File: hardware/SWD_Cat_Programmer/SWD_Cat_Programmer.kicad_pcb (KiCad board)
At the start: 2 copper layers, 40.6 x 28.1 mm, 25 parts, among them J1 DEBUG_OUT, P1 USB_C_Plug_USB2.0, SW1 RST, SW2 BOOT, U1 CH552G, U2 HX9193-33GB

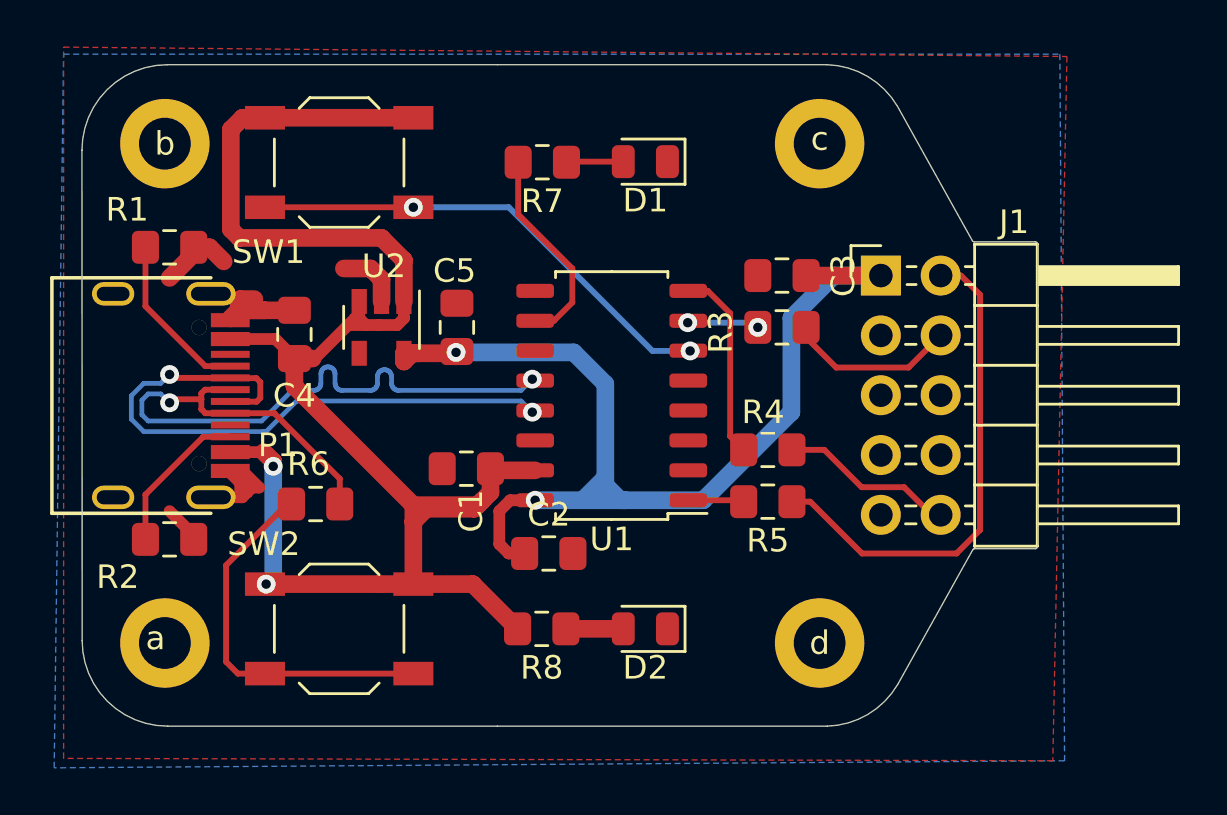
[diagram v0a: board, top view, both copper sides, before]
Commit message: added logos EC
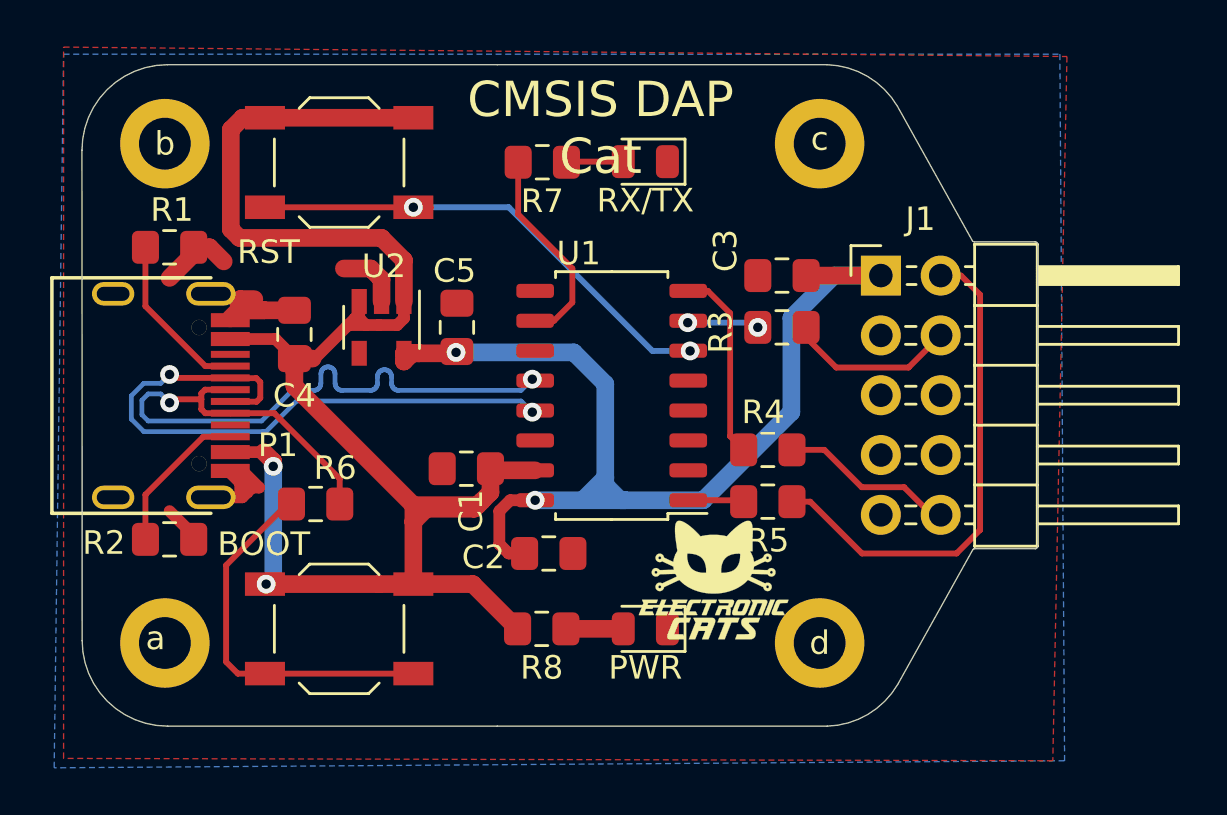
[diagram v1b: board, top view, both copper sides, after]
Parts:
- added G***: LOGO, Aesthetics:electronic_cats_logo_4x3, F.Cu at (158.1, 80.5)
- added G***: LOGO, Aesthetics:electronic_cats_logo_8x6, B.Cu at (149.0, 77.1)
- renumbered SW2 to BOOT, D2 to PWR, SW1 to RST, D1 to RX/TX
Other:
- board text added: "CMSIS DAP Cat"
- board text added: "CMSIS DAP Cat v1.0"

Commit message: labels added
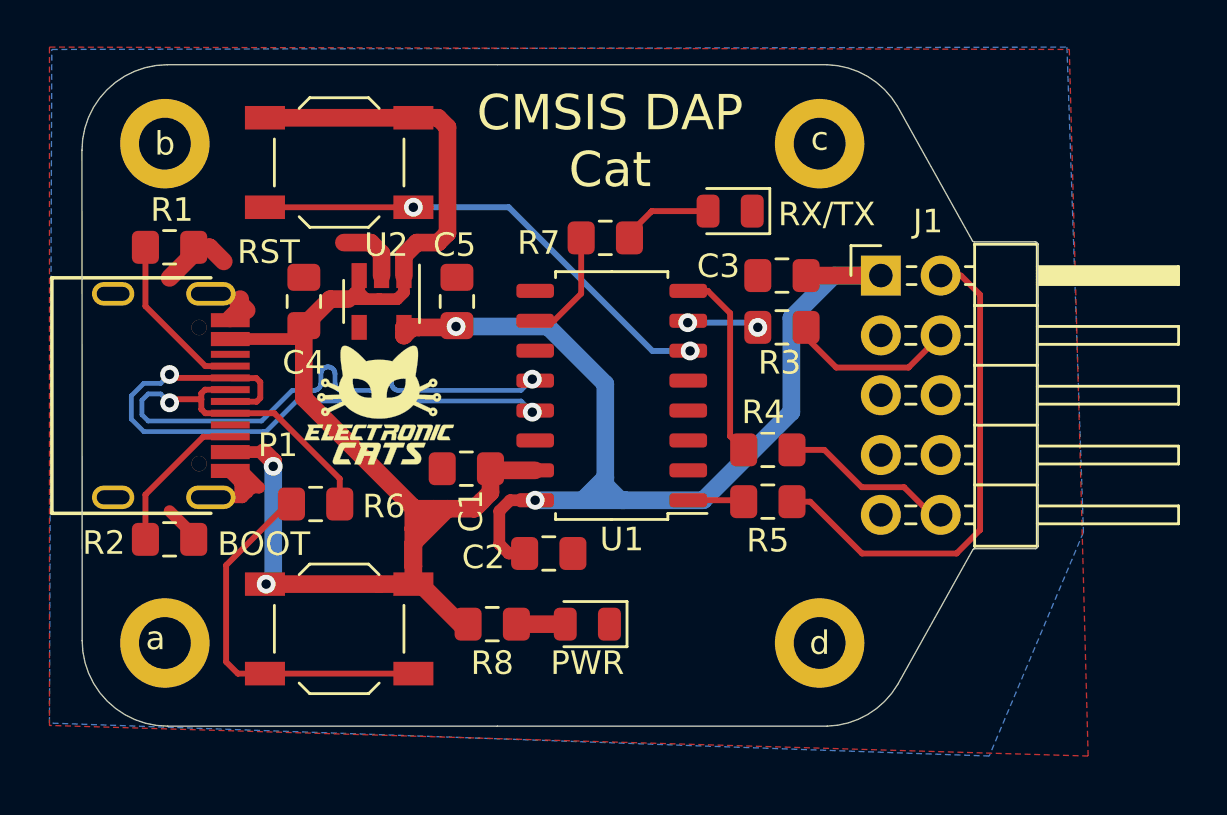
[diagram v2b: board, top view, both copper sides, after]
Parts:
- moved G*** 16.0 mm to (143.9, 73.1)
- moved R7 4.18 mm to (153.5, 66.0)
- moved RX/TX 4.17 mm to (158.8, 64.9)
- moved PWR 2.47 mm to (152.7, 82.4)
- moved R8 2.11 mm to (148.7, 82.4)
- moved C4 1.46 mm to (140.7, 68.7)
- moved C5 1.10 mm to (147.2, 68.7)
- moved U2 1.10 mm to (144.0, 68.7)
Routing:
- net +5V: track 74.3 -> 67.1 mm
- net /LED: track 8.81 -> 4.80 mm
- net GND: track 17.5 -> 13.8 mm
- net Net-(D1-Pad2): track 2.42 -> 3.95 mm
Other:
- board text added: "3V3"
- board text added: "GND"
- board text added: "NC"
- board text added: "RST"
- board text added: "SWC"
- board text added: "SWD"

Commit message: modifed design
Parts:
- removed  a: MountingHole_2.2mm_M2_DIN965_Pad, MountingHole:MountingHole_2.2mm_M2_DIN965_Pad
- removed b, c, d: MountingHole_2.2mm_M2_DIN965_Pad, MountingHole:MountingHole_2.2mm_M2_DIN965_Pad
- moved ON 17.9 mm to (135.2, 79.0)
- moved BOOT 16.8 mm to (143.3, 65.8)
- moved RST 16.8 mm to (143.5, 79.5)
- moved R8 13.4 mm to (135.4, 81.0), turned to 0 degrees
- moved C2 13.4 mm to (148.4, 66.3), turned to 90 degrees
- moved G*** 13.4 mm to (154.7, 65.3)
- moved R2 10.3 mm to (144.8, 75.6), turned to 0 degrees
- moved C1 10.0 mm to (150.5, 66.2), turned to 90 degrees
- moved R7 7.54 mm to (161.0, 65.6)
- moved C4 6.86 mm to (141.0, 75.6), turned to 0 degrees
- moved R6 6.65 mm to (140.5, 70.7), turned to 90 degrees
- moved RX/TX 5.82 mm to (164.6, 64.8)
- moved R5 5.45 mm to (161.0, 71.8)
- moved G*** 4.97 mm to (151.2, 72.6)
- moved C5 2.24 mm to (146.4, 70.8), turned to 270 degrees
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- renumbered PWR to ON
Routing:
- net +5V: track 67.1 -> 87.4 mm, vias 2 -> 4
- net +3V3: track 46.0 -> 29.8 mm, vias 2 -> 1
- net Net-(R5-Pad2): track 2.38 -> 13.0 mm
- net /SWDIO: track 21.3 -> 11.2 mm
- net Net-(R3-Pad2): track 3.28 -> 12.6 mm, vias 2 -> 0
- net Net-(R6-Pad2): track 16.2 -> 8.35 mm
- net Net-(R4-Pad2): track 8.21 -> 3.62 mm
- net Net-(P1-PadB5): track 6.52 -> 10.8 mm
- net GND: track 13.8 -> 17.4 mm
- net /RST: track 21.3 -> 18.6 mm, vias 2 -> 0
- net /D-: track 26.9 -> 29.4 mm
- net Net-(D1-Pad2): track 3.95 -> 1.98 mm
- net /RESET: track 7.46 -> 8.57 mm
- net /LED: track 4.80 -> 5.61 mm
- net Net-(P1-PadA5): track 7.16 -> 7.71 mm
- added copper zone on B.Cu, net (none)
- added copper zone on F.Cu, net (none)
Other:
- board size 40.6 x 28.1 mm -> 40.5 x 20.1 mm

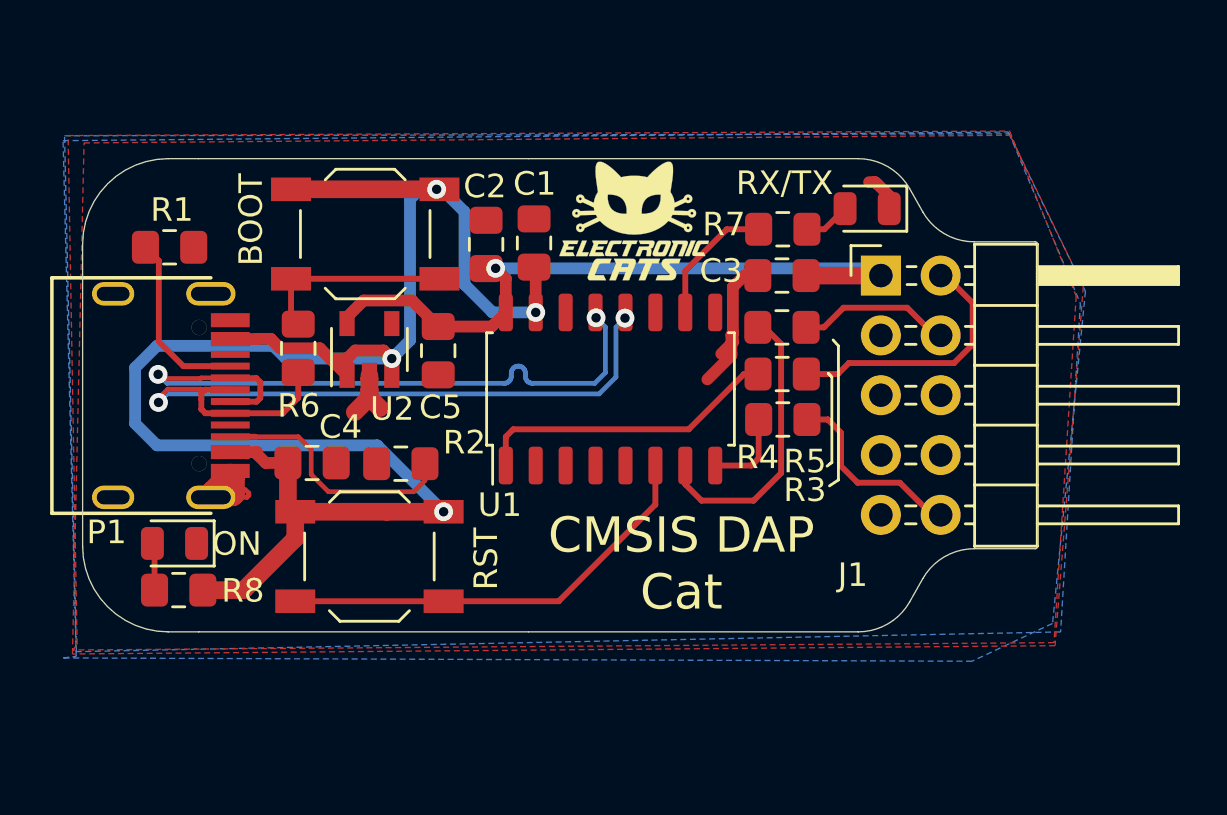
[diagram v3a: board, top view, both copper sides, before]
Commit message: Pull up Resistors Update
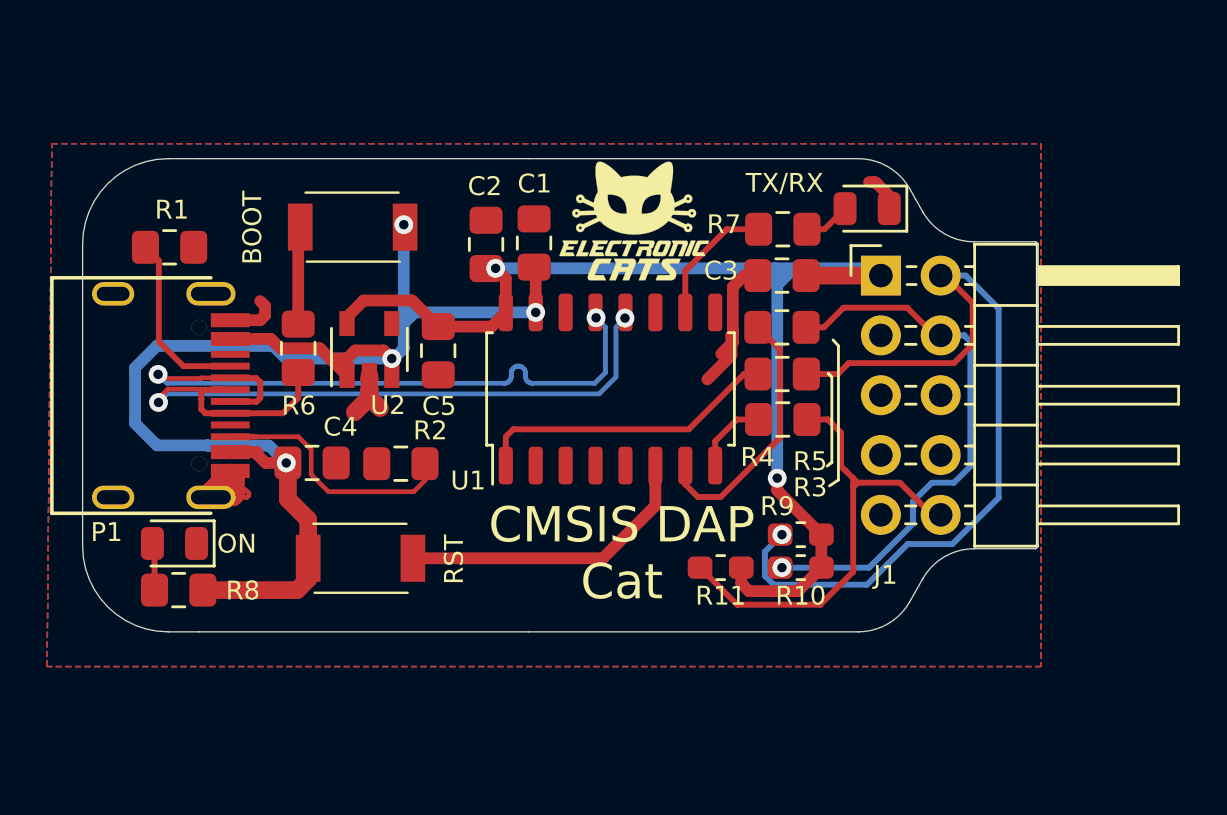
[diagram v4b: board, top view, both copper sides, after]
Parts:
- removed the BOOT at (143.3, 65.8)
- removed the RST at (143.5, 79.5)
- added BOOT: BOOT, KiCad:TS1088R02026, F.Cu at (142.8, 65.5)
- added R10: 70, Resistor_SMD:R_0603_1608Metric_Pad1.05x0.95mm_HandSolder, F.Cu at (161.8, 80.0)
- added R11: 70, Resistor_SMD:R_0603_1608Metric_Pad1.05x0.95mm_HandSolder, F.Cu at (158.4, 80.0)
- added R9: 70, Resistor_SMD:R_0603_1608Metric_Pad1.05x0.95mm_HandSolder, F.Cu at (161.8, 78.6)
- added RST: RST, KiCad:TS1088R02026, F.Cu at (143.1, 79.6)
- renumbered RX/TX to TX/RX
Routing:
- net +5V: track 87.4 -> 58.5 mm
- net /SWDIO: track 11.2 -> 35.9 mm, vias 0 -> 1
- net +3V3: track 29.8 -> 49.9 mm, vias 1 -> 2
- net /SWCLK: track 6.97 -> 24.0 mm, vias 0 -> 1
- net /RESET: track 8.57 -> 21.0 mm
- net /RST: track 18.6 -> 13.7 mm
- net Net-(R6-Pad2): track 8.35 -> 4.16 mm
- net GND: track 17.4 -> 19.6 mm
- net Net-(R3-Pad2): track 12.6 -> 11.7 mm

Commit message: Jumper
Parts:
- added JP1: Jumper, Jumper:SolderJumper-3_P1.3mm_Bridged12_RoundedPad1.0x1.5mm, B.Cu at (154.7, 65.6)
- renumbered TX/RX to D1, ON to D2, RST to SW1, BOOT to SW2
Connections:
- C1 pad 1: +5V -> Net-(C1-Pad1)
- U1 pad 15: +5V -> Net-(C1-Pad1)
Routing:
- net Net-(C1-Pad1): track 0.00 -> 7.72 mm, vias 0 -> 1
- net +3V3: track 49.9 -> 53.6 mm
- net +5V: track 58.5 -> 59.6 mm, vias 4 -> 3

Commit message: update label
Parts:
- renumbered SW2 to BOOT, D2 to PWR, SW1 to RST, D1 to TX/RX
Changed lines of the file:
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@@
-(kicad_pcb (version 20171130) (host pcbnew "(5.1.6)-1")
+(kicad_pcb (version 20171130) (host pcbnew "(5.1.5-0-10_14)")
   (general
     (thickness 1.6)
@@
   )
   (page A4)
+  (title_block
+    (title "CMSIS DAP Cat")
+    (date 2020-08-08)
+    (rev 1.0)
+    (company "Electronic Cats")
+    (comment 2 "Felipe Islas")
+    (comment 3 "Eduaro Wero")
+    (comment 4 "Andres Sabas")
+  )
   (layers
     (0 F.Cu signal)
@@
     (35 F.Paste user)
     (36 B.SilkS user)
-    (37 F.SilkS user hide)
-    (38 B.Mask user hide)
-    (39 F.Mask user hide)
+    (37 F.SilkS user)
+    (38 B.Mask user)
+    (39 F.Mask user)
     (40 Dwgs.User user)
     (41 Cmts.User user)
@@
   )
   (setup
-    (last_trace_width 0.5)
+    (last_trace_width 0.25)
     (user_trace_width 0.2)
     (user_trace_width 0.5)
@@
     (tags Switch)
     (attr smd)
-    (fp_text reference SW2 (at 4.25704 -0.02794 90) (layer F.SilkS)
+    (fp_text reference BOOT (at 4.25704 -0.02794 90) (layer F.SilkS)
       (effects (font (size 0.8 0.8) (thickness 0.12)))
     )
@@
     (tags Switch)
     (attr smd)
-    (fp_text reference SW1 (at 3.97256 0.05334 270) (layer F.SilkS)
+    (fp_text reference RST (at 3.97256 0.05334 270) (layer F.SilkS)
       (effects (font (size 0.8 0.8) (thickness 0.12)))
     )
@@
     (tags "resistor handsolder")
     (attr smd)
-    (fp_text reference R7 (at 2.49936 0.20574) (layer F.SilkS)
+    (fp_text reference R7 (at 2.526 -0.0964) (layer F.SilkS)
       (effects (font (size 0.8 0.8) (thickness 0.12)))
     )
@@
     (tags diode)
     (attr smd)
-    (fp_text reference D2 (at -2.64668 -0.01778) (layer F.SilkS)
+    (fp_text reference PWR (at -3.05072 -0.05632) (layer F.SilkS)
       (effects (font (size 0.8 0.8) (thickness 0.12)))
     )
@@
     (tags diode)
     (attr smd)
-    (fp_text reference D1 (at 3.50266 1.08458) (layer F.SilkS)
+    (fp_text reference TX/RX (at 3.6474 0.6873) (layer F.SilkS)
       (effects (font (size 0.8 0.8) (thickness 0.12)))
     )
@@
   (gr_line (start 150.236401 82.727286) (end 164.236401 82.727286) (layer Edge.Cuts) (width 0.05))
   (gr_line (start 150.2364 62.6364) (end 164.2364 62.6364) (layer Edge.Cuts) (width 0.05))
-  (via (at 154.7 65.6) (size 0.8) (drill 0.4) (layers F.Cu B.Cu) (net 30))
   (segment (start 137.5786 75.8948) (end 138.0948 75.8948) (width 0.5) (layer F.Cu) (net 1))
   (segment (start 165.5549 64.7573) (end 165.5549 64.21604) (width 0.5) (layer F.Cu) (net 1))
@@
   (segment (start 138.1052 75.0948) (end 138.155199 75.044801) (width 0.5) (layer F.Cu) (net 2))
   (segment (start 137.5786 75.0948) (end 138.1052 75.0948) (width 0.5) (layer F.Cu) (net 2))
-  (segment (start 150.5458 67.4206) (end 150.5757 67.3907) (width 0.5) (layer F.Cu) (net 30))
-  (segment (start 150.5458 69.1654) (end 150.5458 69.1654) (width 0.5) (layer F.Cu) (net 30))
   (segment (start 137.5786 70.2948) (end 138.713602 70.2948) (width 0.5) (layer F.Cu) (net 2))
   (segment (start 137.5786 75.0948) (end 138.713602 75.0948) (width 0.5) (layer F.Cu) (net 2))
@@
   (segment (start 138.721522 70.28688) (end 138.713602 70.2948) (width 0.5) (layer F.Cu) (net 2))
   (segment (start 139.29868 70.28688) (end 139.7 70.6882) (width 0.5) (layer F.Cu) (net 2))
-  (segment (start 150.5757 67.3907) (end 150.7236 67.2428) (width 0.5) (layer F.Cu) (net 30))
   (segment (start 142.5346 71.123998) (end 142.878958 70.77964) (width 0.5) (layer F.Cu) (net 2))
   (segment (start 142.5346 71.839) (end 142.5346 71.123998) (width 0.5) (layer F.Cu) (net 2))
@@
   (segment (start 133.53542 73.87844) (end 133.53542 71.515538) (width 0.5) (layer B.Cu) (net 2))
   (segment (start 134.466779 74.809799) (end 133.53542 73.87844) (width 0.5) (layer B.Cu) (net 2))
-  (segment (start 150.5458 69.1654) (end 150.5458 67.4206) (width 0.5) (layer F.Cu) (net 30))
   (segment (start 140.88368 80.48748) (end 140.88368 79.6036) (width 0.75) (layer F.Cu) (net 2))
   (segment (start 136.41208 80.95488) (end 140.41628 80.95488) (width 0.75) (layer F.Cu) (net 2))
@@
   (segment (start 155.6258 77.3742) (end 155.6258 75.6654) (width 0.5) (layer F.Cu) (net 22))
   (segment (start 153.3964 79.6036) (end 155.6258 77.3742) (width 0.5) (layer F.Cu) (net 22))
+  (via (at 154.7 65.6) (size 0.8) (drill 0.4) (layers F.Cu B.Cu) (net 30))
+  (segment (start 150.5458 67.4206) (end 150.5757 67.3907) (width 0.5) (layer F.Cu) (net 30))
+  (segment (start 150.5458 69.1654) (end 150.5458 69.1654) (width 0.5) (layer F.Cu) (net 30))
+  (segment (start 150.5757 67.3907) (end 150.7236 67.2428) (width 0.5) (layer F.Cu) (net 30))
+  (segment (start 150.5458 69.1654) (end 150.5458 67.4206) (width 0.5) (layer F.Cu) (net 30))
   (segment (start 154.7 65.6) (end 154.7 66) (width 0.5) (layer F.Cu) (net 30))
   (segment (start 150.47468 66.52532) (end 150.47468 67.2428) (width 0.5) (layer F.Cu) (net 30))
